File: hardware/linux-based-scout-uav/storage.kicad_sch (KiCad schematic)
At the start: 1 part, among them J2 Micro_SD_Card_Det2

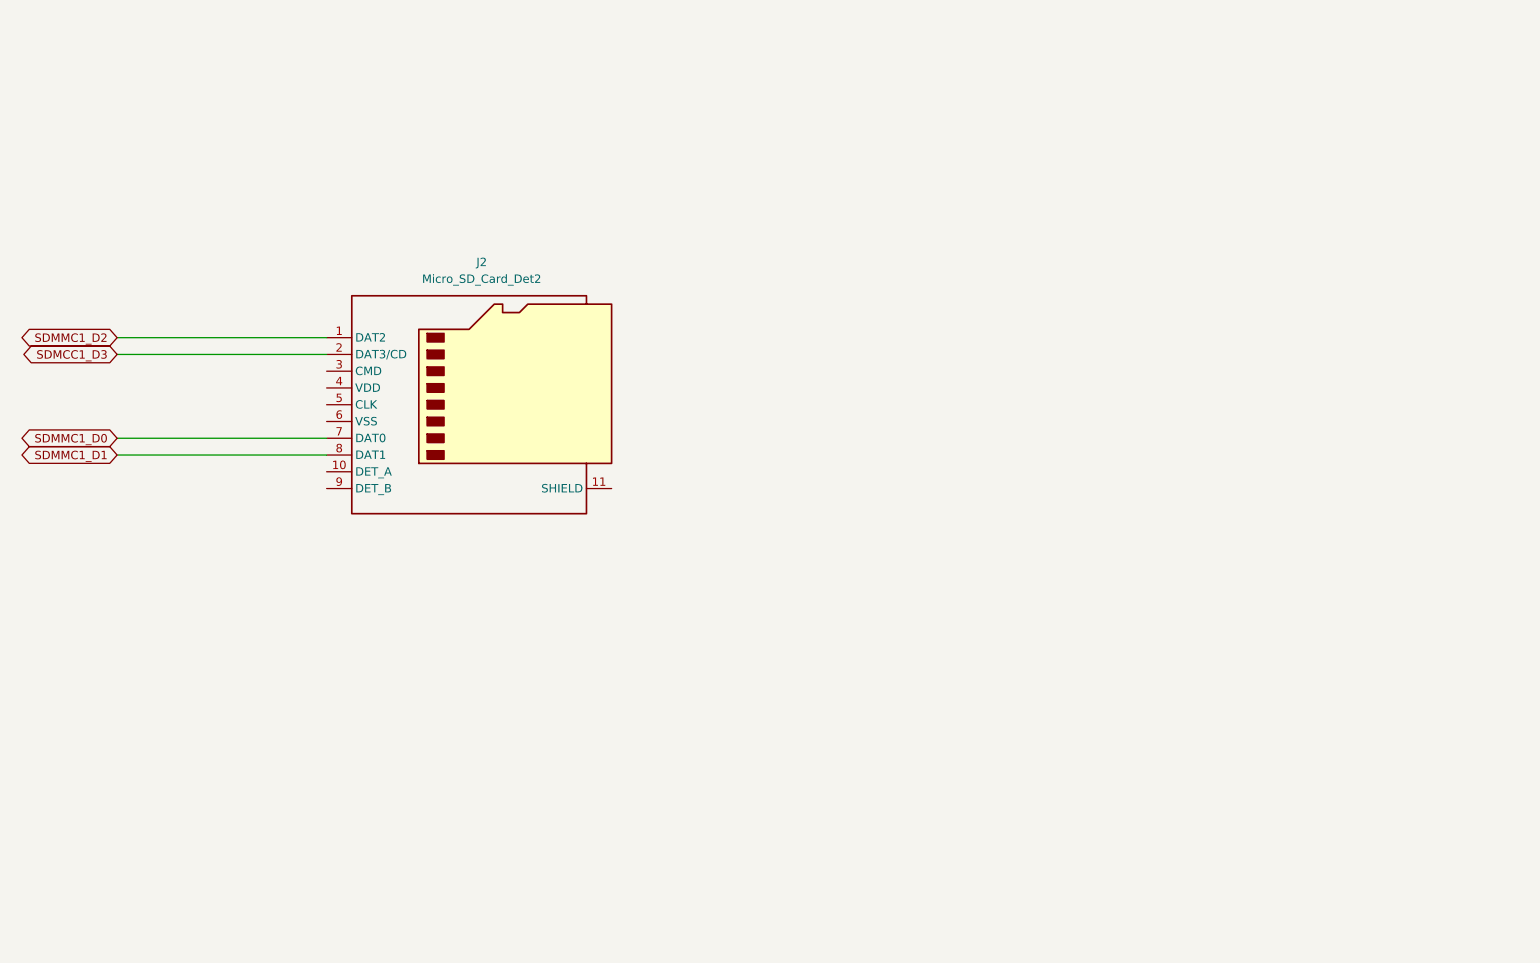
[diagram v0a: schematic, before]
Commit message: Updates (schematic, readme, doc files, device tree)
Updates to schematic, readme file and doc files.
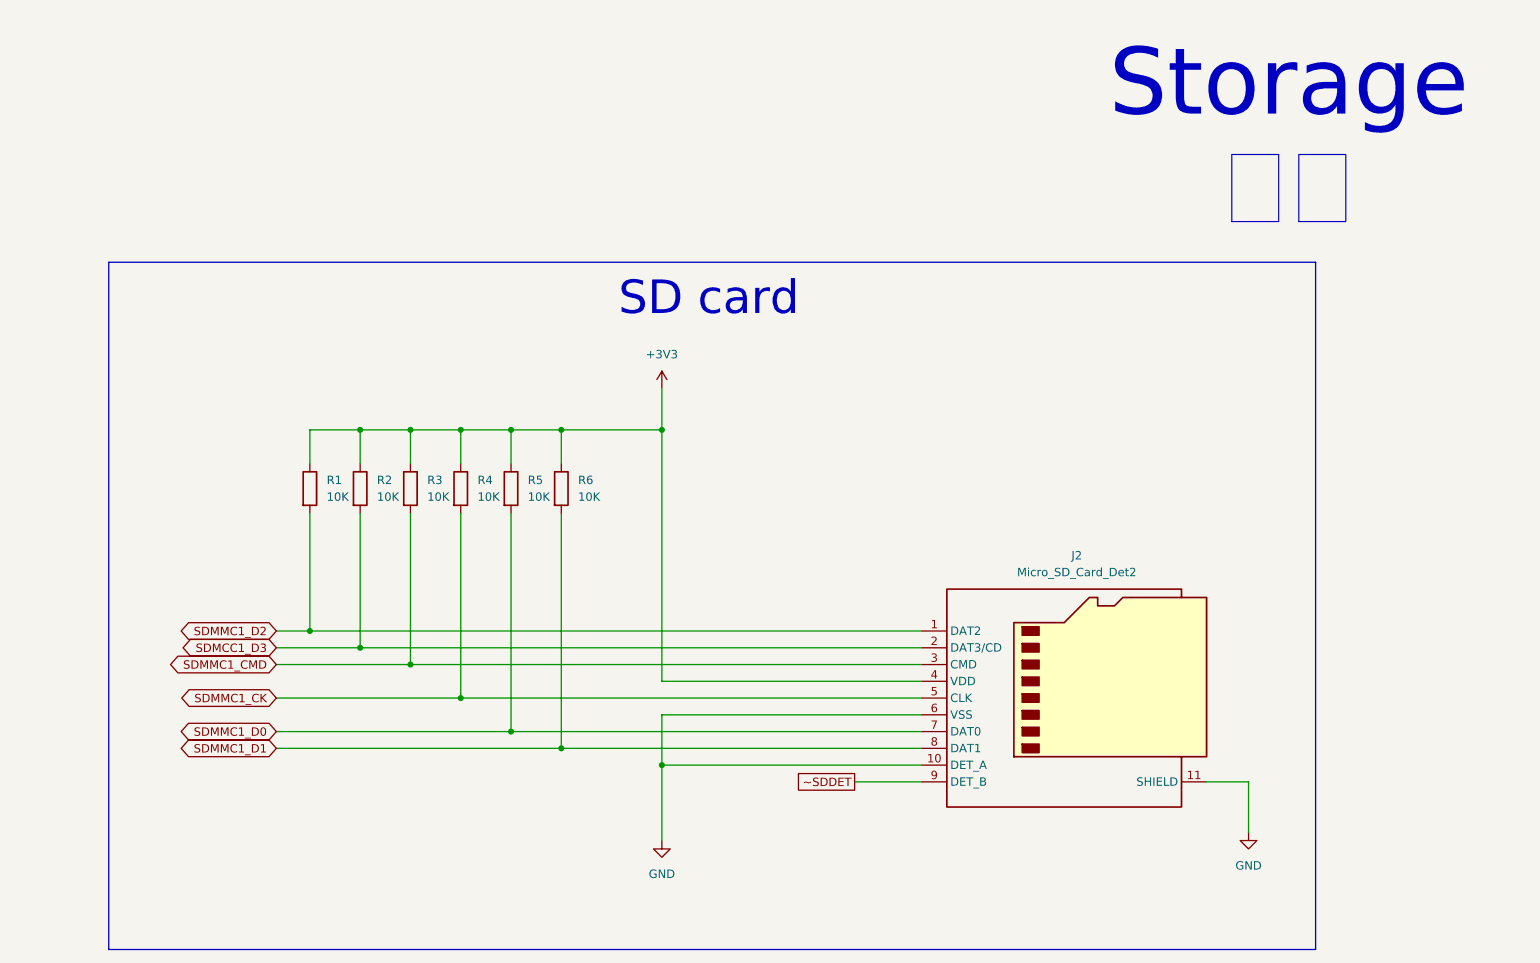
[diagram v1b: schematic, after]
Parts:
- added R1, R2, R3, R4, R5, R6: 10K, Resistor_SMD:R_0201_0603Metric, symbol Device:R
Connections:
- net SDMCC1_D3: now also R2.2
- net SDMMC1_D0: now also R5.2
- net SDMMC1_D1: now also R6.2
- net SDMMC1_D2: now also R1.2
- net GND: now reaches J2.10 (DET_A)
- net GND: now also J2.11 (SHIELD), J2.6 (VSS)
- net SDMMC1_CMD: now reaches J2.3 (CMD)
- net SDMMC1_CMD: now also R3.2
- net +3V3: now reaches J2.4 (VDD)
- net +3V3: now also R1.1, R2.1, R3.1, R4.1, R5.1, R6.1
- net SDMMC1_CK: now reaches J2.5 (CLK)
- net SDMMC1_CK: now also R4.2
- net ~SDDET: now reaches J2.9 (DET_B)
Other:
- note added: "SD card"
- note added: "Storage 貯蔵"
- moved on the sheet: J2

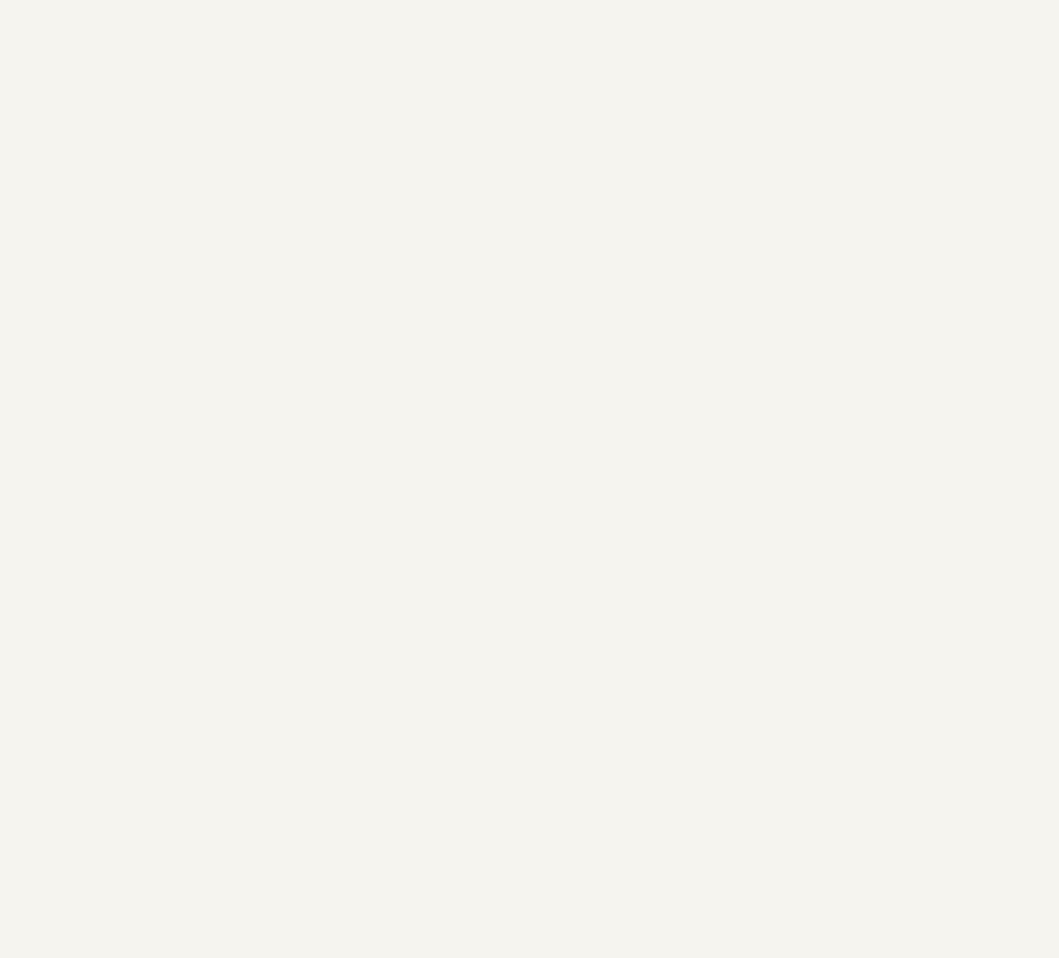
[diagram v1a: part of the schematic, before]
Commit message: Schematic update - eMMC added
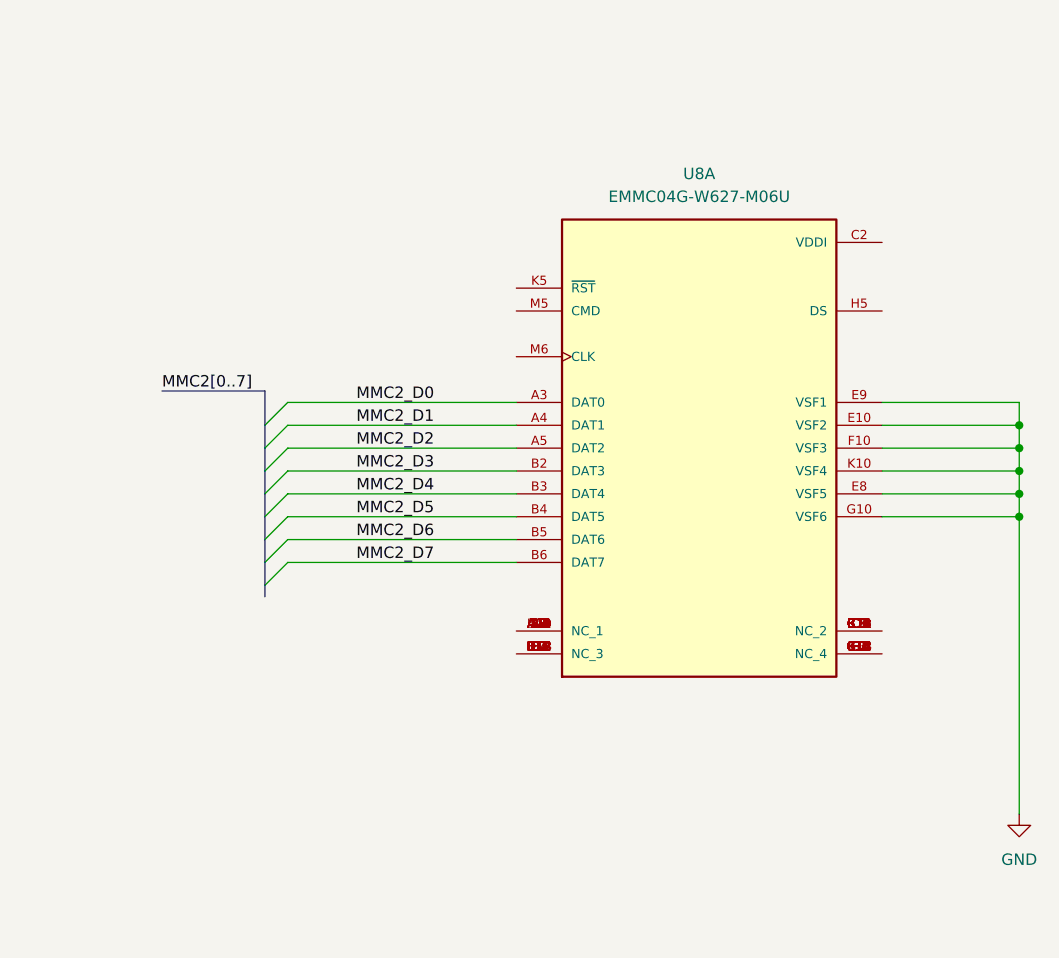
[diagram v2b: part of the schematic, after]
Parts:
- added U8: EMMC04G-W627-M06U, EMMC04G-W627-M06U:BGA153N50P14X14_1300X1150X100N, symbol EMMC04G-W627-M06U:EMMC04G-W627-M06U
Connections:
- net GND: now also U8.E10 (VSF2), U8.E8 (VSF5), U8.E9 (VSF1), U8.F10 (VSF3), U8.G10 (VSF6), U8.K10 (VSF4)
- new net: U8.A1 (NC_1), U8.A10 (NC_1), U8.A11 (NC_1), U8.A12 (NC_1), U8.A13 (NC_1), U8.A14 (NC_1), U8.A2 (NC_1), U8.A8 (NC_1), U8.A9 (NC_1), U8.B1 (NC_1), U8.B10 (NC_1), U8.B7 (NC_1), U8.B8 (NC_1), U8.B9 (NC_1)
- new net: U8.B11 (NC_2), U8.B12 (NC_2), U8.B13 (NC_2), U8.B14 (NC_2), U8.C1 (NC_2), U8.C10 (NC_2), U8.C11 (NC_2), U8.C12 (NC_2), U8.C13 (NC_2), U8.C14 (NC_2), U8.C3 (NC_2), U8.C5 (NC_2), U8.C7 (NC_2), U8.C8 (NC_2), U8.C9 (NC_2)
- new net: U8.D1 (NC_3), U8.D12 (NC_3), U8.D13 (NC_3), U8.D14 (NC_3), U8.D2 (NC_3), U8.D3 (NC_3), U8.D4 (NC_3), U8.E1 (NC_3), U8.E12 (NC_3), U8.E13 (NC_3), U8.E2 (NC_3), U8.E3 (NC_3)
- new net: U8.E14 (NC_4), U8.F1 (NC_4), U8.F12 (NC_4), U8.F13 (NC_4), U8.F14 (NC_4), U8.F2 (NC_4), U8.F3 (NC_4), U8.G1 (NC_4), U8.G12 (NC_4), U8.G13 (NC_4), U8.G14 (NC_4), U8.G2 (NC_4)
- new net MMC2_D0: U8.A3 (DAT0)
- new net MMC2_D1: U8.A4 (DAT1)
- new net MMC2_D2: U8.A5 (DAT2)
- new net MMC2_D3: U8.B2 (DAT3)
- new net MMC2_D4: U8.B3 (DAT4)
- new net MMC2_D5: U8.B4 (DAT5)
- new net MMC2_D6: U8.B5 (DAT6)
- new net MMC2_D7: U8.B6 (DAT7)

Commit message: Schematic/board update
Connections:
- net SDMCC1_D3 renamed SDMMC1_D3
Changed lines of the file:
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@@
+		)
+	)
+	(bus
+		(pts
+			(xy 261.62 91.44) (xy 274.32 91.44)
+		)
+		(stroke
+			(width 0)
+			(type default)
 		)
 	)
@@
 		(pts
 			(xy 342.9 97.79) (xy 358.14 97.79)
-		)
-		(stroke
-			(width 0)
-			(type default)
-		)
-	)
-	(bus
-		(pts
-			(xy 262.89 91.44) (xy 274.32 91.44)
 		)
 		(stroke
@@
 			(justify left bottom)
 		)
-	)
-	(label "MMC2[0..7]"
-		(at 262.89 91.44 0)
-		(fields_autoplaced yes)
-		(effects
-			(font
-				(size 1.27 1.27)
-			)
-			(justify left bottom)
+		(property "MMC2_D1" ""
+			(at 284.48 96.52 0)
+			(effects
+				(font
+					(size 1.27 1.27)
+					(italic yes)
+				)
+				(justify left)
+			)
 		)
 	)
@@
 			)
 			(justify left bottom)
+		)
+		(property "MMC2_D0" ""
+			(at 284.48 93.98 0)
+			(effects
+				(font
+					(size 1.27 1.27)
+					(italic yes)
+				)
+				(justify left)
+			)
 		)
 	)
@@
 		)
 	)
-	(global_label "SDMCC1_D3"
+	(global_label "MMC2_D[0..7]"
+		(shape input)
+		(at 261.62 91.44 180)
+		(fields_autoplaced yes)
+		(effects
+			(font
+				(size 1.27 1.27)
+			)
+			(justify right)
+		)
+		(property "Intersheetrefs" "${INTERSHEET_REFS}"
+			(at 245.6929 91.44 0)
+			(effects
+				(font
+					(size 1.27 1.27)
+				)
+				(justify right)
+				(hide yes)
+			)
+		)
+	)
+	(global_label "SDMMC1_D3"
 		(shape bidirectional)
 		(at 58.42 106.68 180)
@@
 		)
 		(property "Intersheetrefs" "${INTERSHEET_REFS}"
-			(at 43.196 106.68 0)
+			(at 43.0146 106.68 0)
 			(effects
 				(font

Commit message: Schematic update
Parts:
- added R26, R27, R28, R29, R30, R31, R32, R33, R34: 10K, symbol Device:R
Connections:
- net +3V3: now also R26.1, R27.1, R28.1, R29.1, R30.1, R31.1, R32.1, R33.1, R34.1
- net MMC2_D0: now also R26.2
- net MMC2_D1: now also R27.2
- net MMC2_D2: now also R28.2
- net MMC2_D3: now also R29.2
- net MMC2_D4: now also R30.2
- net MMC2_D5: now also R31.2
- net MMC2_D6: now also R32.2
- net MMC2_D7: now also R33.2
- net NRST: now reaches U8.K5 (~{RST})
- net NRST: now also R34.2
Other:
- note added: "eMMC"
- moved on the sheet: U8A

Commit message: Schematic update
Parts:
- added C10, C11, C8, C9: 0.1uF, symbol Device:C
- added C12: C, symbol Device:C
- added C7: 10uF, symbol Device:C
- added R35: 10K, symbol Device:R
- added TP19: TestPoint, symbol Connector:TestPoint
- added unit 2 of U8
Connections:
- net +3V3: now also C10.1, C11.1, C7.1, C8.1, C9.1, R35.1, U8.C6 (VCCQ), U8.E6 (VCC), U8.F5 (VCC), U8.J10 (VCC), U8.K9 (VCC), U8.M4 (VCCQ), U8.N4 (VCCQ), U8.P3 (VCCQ), U8.P5 (VCCQ)
- net GND: now also C10.2, C11.2, C12.2, C7.2, C8.2, C9.2, U8.A6 (VSS), U8.C4 (VSSQ), U8.E7 (VSS), U8.G5 (VSS), U8.H10 (VSS), U8.J5 (VSS), U8.K8 (VSS), U8.N2 (VSSQ), U8.N5 (VSSQ), U8.P4 (VSSQ), U8.P6 (VSSQ); no longer U8.E10 (VSF2), U8.E8 (VSF5), U8.E9 (VSF1), U8.F10 (VSF3), U8.G10 (VSF6), U8.K10 (VSF4)
- net at U8.C2 (VDDI): now also C12.1
- net at U8.H5 (DS): now also TP19.1
- net MMC2_CMD: now reaches U8.M5 (CMD)
- net MMC2_CMD: now also R35.2
- net MMC2_CLK: now reaches U8.M6 (CLK)
- new net: U8.H1 (NC_5), U8.H12 (NC_5), U8.H13 (NC_5), U8.H14 (NC_5), U8.H2 (NC_5), U8.H3 (NC_5), U8.J1 (NC_5), U8.J12 (NC_5), U8.J13 (NC_5), U8.J14 (NC_5), U8.J2 (NC_5), U8.J3 (NC_5), U8.K1 (NC_5), U8.K2 (NC_5), U8.K3 (NC_5)
- new net: U8.K12 (NC_6), U8.K13 (NC_6), U8.K14 (NC_6), U8.L1 (NC_6), U8.L12 (NC_6), U8.L13 (NC_6), U8.L14 (NC_6), U8.L2 (NC_6), U8.L3 (NC_6), U8.M1 (NC_6), U8.M2 (NC_6), U8.M3 (NC_6), U8.M7 (NC_6)
- new net: U8.M10 (NC_7), U8.M11 (NC_7), U8.M12 (NC_7), U8.M13 (NC_7), U8.M14 (NC_7), U8.M8 (NC_7), U8.M9 (NC_7), U8.N1 (NC_7), U8.N10 (NC_7), U8.N3 (NC_7), U8.N6 (NC_7), U8.N7 (NC_7), U8.N8 (NC_7), U8.N9 (NC_7)
- new net: U8.N11 (NC_8), U8.N12 (NC_8), U8.N13 (NC_8), U8.N14 (NC_8), U8.P1 (NC_8), U8.P11 (NC_8), U8.P12 (NC_8), U8.P13 (NC_8), U8.P14 (NC_8), U8.P2 (NC_8), U8.P8 (NC_8), U8.P9 (NC_8)
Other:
- note added: "eMMC power"
- moved on the sheet: R26, R27, R28, R29, R30, R31, R32, R33, R34, U8A
